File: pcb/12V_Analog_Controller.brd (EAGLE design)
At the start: 50 x 36 mm, 32 parts, among them J1 POWER, Q1 AO3400, Q2 AO3400, U1 ESP32-PICO-MINI-02, X1 PROG, X2 L1, X3 L2, X5 BOOT, X6 RESET

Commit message: Add second PTC footprint
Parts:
- added F3, F4: JK-SMD300L-24, M2M-Fuse:JK-SMD300
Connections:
- net N$5: now also F3.B
- net N$6: now also F4.B
- net VSW: now also F3.A, F4.A
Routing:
- net VSW: track 70.8 -> 79.6 mm
- net N$6: track 5.83 -> 12.8 mm
- net N$5: track 6.24 -> 13.2 mm
- net EN: track 27.3 -> 28.2 mm
- net L2: track 17.0 -> 17.9 mm
- net L1: track 17.5 -> 16.9 mm
- net VCC: track 35.3 -> 35.2 mm, vias 4 -> 3
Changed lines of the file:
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@@
 <drawing>
 <settings>
-<setting alwaysvectorfont="yes"/>
+<setting alwaysvectorfont="no"/>
 <setting verticaltext="up"/>
 </settings>
@@
 </element>
 <element name="X5" library="M2M-Connectors" package="1X02-2.54" value="BOOT" x="25.5" y="3.5" smashed="yes">
-<attribute name="NAME" x="24.23" y="5.0875" size="1.016" layer="25"/>
 <attribute name="NAME" x="24.611" y="2.865" size="1.27" layer="48"/>
 <attribute name="NAME" x="24.865" y="2.865" size="0.8128" layer="51"/>
+<attribute name="NAME" x="24.23" y="5.0875" size="1.016" layer="25"/>
 <attribute name="VALUE" x="24.23" y="0.96" size="1.016" layer="21"/>
 </element>
 <element name="X6" library="M2M-Connectors" package="1X02-2.54" value="RESET" x="19" y="3.5" smashed="yes">
-<attribute name="NAME" x="17.73" y="5.0875" size="1.016" layer="25"/>
 <attribute name="NAME" x="18.111" y="2.865" size="1.27" layer="48"/>
 <attribute name="NAME" x="18.865" y="2.365" size="0.8128" layer="51"/>
+<attribute name="NAME" x="17.73" y="5.0875" size="1.016" layer="25"/>
 <attribute name="VALUE" x="17.73" y="0.96" size="1.016" layer="21"/>
 </element>
@@
 <attribute name="NAME" x="34" y="7.8" size="1.016" layer="21"/>
 <attribute name="VALUE" x="34" y="4.2" size="1.016" layer="27"/>
+</element>
+<element name="F3" library="M2M-Fuse" package="JK-SMD300" value="JK-SMD300L-24" x="21" y="25" smashed="yes" rot="MR90">
+<attribute name="NAME" x="24.5" y="20" size="1.016" layer="26" rot="MR90"/>
+<attribute name="NAME" x="21" y="25" size="1.016" layer="48" rot="MR90" align="center"/>
+<attribute name="VALUE" x="16.5" y="20" size="1.016" layer="28" rot="MR90"/>
+</element>
+<element name="F4" library="M2M-Fuse" package="JK-SMD300" value="JK-SMD300L-24" x="21" y="11" smashed="yes" rot="MR90">
+<attribute name="NAME" x="24.5" y="6" size="1.016" layer="26" rot="MR90"/>
+<attribute name="NAME" x="21" y="11" size="1.016" layer="48" rot="MR90" align="center"/>
+<attribute name="VALUE" x="16.5" y="6" size="1.016" layer="28" rot="MR90"/>
 </element>
 </elements>
@@
 <vertex x="20.3" y="11.7"/>
 </polygon>
-<wire x1="22.5" y1="12.35" x2="22.5" y2="13.1298" width="0.254" layer="1"/>
-<via x="22.5" y="13.1298" extent="1-16" drill="0.35"/>
 <via x="27.5" y="11.5" extent="1-16" drill="0.35"/>
 <wire x1="27.5" y1="11.5" x2="27.15" y2="10.85" width="0.254" layer="1"/>
 <wire x1="27.15" y1="10.85" x2="26.5" y2="10.85" width="0.254" layer="1"/>
-<wire x1="22.5" y1="13.1298" x2="22.6298" y2="13" width="0.254" layer="16"/>
-<wire x1="26" y1="13" x2="27.5" y2="11.5" width="0.254" layer="16"/>
-<wire x1="26" y1="13" x2="22.6298" y2="13" width="0.254" layer="16"/>
 <wire x1="20.5" y1="12.35" x2="19.5" y2="11.35" width="0.254" layer="1"/>
 <wire x1="19.5" y1="7.85" x2="20" y2="7.35" width="0.254" layer="1"/>
@@
 <wire x1="28.1" y1="26.9" x2="25.75" y2="26.9" width="0.6096" layer="1"/>
 <wire x1="25.75" y1="26.9" x2="25.5" y2="26.65" width="0.6096" layer="1"/>
-<wire x1="20.5" y1="12.35" x2="20.5" y2="13" width="0.6096" layer="1"/>
-<via x="20.5" y="13" extent="1-16" drill="0.35"/>
-<wire x1="20.5" y1="23" x2="20.5" y2="13" width="0.6096" layer="16"/>
-<wire x1="20.5" y1="23" x2="24" y2="26.5" width="0.6096" layer="16"/>
 <via x="24" y="26.5" extent="1-16" drill="0.35"/>
 <wire x1="24" y1="26.5" x2="24.15" y2="26.65" width="0.6096" layer="1"/>
 <wire x1="24.15" y1="26.65" x2="25.5" y2="26.65" width="0.6096" layer="1"/>
+<wire x1="20.5" y1="12.35" x2="21.35" y2="12.35" width="0.6096" layer="1"/>
+<wire x1="21.35" y1="12.35" x2="21.5" y2="12.5" width="0.6096" layer="1"/>
+<via x="21.5" y="12.5" extent="1-16" drill="0.35"/>
+<wire x1="21.5" y1="12.5" x2="23.5" y2="12.5" width="0.6096" layer="16"/>
+<wire x1="23.5" y1="12.5" x2="23.75" y2="12.75" width="0.6096" layer="16"/>
+<wire x1="23.75" y1="12.75" x2="24.5" y2="13.5" width="0.6096" layer="16"/>
+<wire x1="24.5" y1="26" x2="24" y2="26.5" width="0.6096" layer="16"/>
+<wire x1="24.5" y1="13.5" x2="24.5" y2="26" width="0.6096" layer="16"/>
+<wire x1="27.5" y1="11.5" x2="26.25" y2="12.75" width="0.254" layer="16"/>
+<wire x1="26.25" y1="12.75" x2="23.75" y2="12.75" width="0.254" layer="16"/>
 </signal>
 <signal name="GND">
@@
 <via x="40" y="18.5" extent="1-16" drill="0.35"/>
 <via x="31" y="18.5" extent="1-16" drill="0.35"/>
-<via x="27.119" y="19.643" extent="1-16" drill="0.35"/>
+<via x="28.119" y="18.643" extent="1-16" drill="0.35"/>
 <via x="47.5" y="2.5" extent="1-16" drill="0.35"/>
 <via x="46" y="23" extent="1-16" drill="0.35"/>
@@
 <via x="10.5" y="27" extent="1-16" drill="0.35"/>
 <via x="32" y="16" extent="1-16" drill="0.35"/>
-<via x="23.5" y="8" extent="1-16" drill="0.35"/>
+<via x="25.5" y="8.5" extent="1-16" drill="0.35"/>
 <via x="29.5" y="7" extent="1-16" drill="0.35"/>
-<via x="18.5" y="8.5" extent="1-16" drill="0.35"/>
-<via x="18.5" y="22.5" extent="1-16" drill="0.35"/>
+<via x="18" y="9" extent="1-16" drill="0.35"/>
+<via x="19.5" y="24" extent="1-16" drill="0.35"/>
 <contactref element="C2" pad="2"/>
 <contactref element="U$3" pad="2"/>
@@
 <contactref element="R8" pad="1"/>
 <contactref element="C4" pad="2"/>
+<via x="19" y="12.5" extent="1-16" drill="0.35"/>
 </signal>
 <signal name="IO0">
@@
 <wire x1="19" y1="3.5" x2="20" y2="4.5" width="0.254" layer="1"/>
 <wire x1="20" y1="4.5" x2="20" y2="5.65" width="0.254" layer="1"/>
-<wire x1="26.5" y1="22" x2="26.5" y2="20" width="0.254" layer="1"/>
-<wire x1="25.5" y1="19" x2="24" y2="19" width="0.254" layer="1"/>
-<wire x1="24" y1="19" x2="17.5" y2="12.5" width="0.254" layer="1"/>
-<wire x1="17.5" y1="12.5" x2="17.497340625" y2="12.002659375" width="0.254" layer="1"/>
+<wire x1="26.5" y1="19.5" x2="26.5" y2="22" width="0.254" layer="1"/>
 <via x="17.497340625" y="12.002659375" extent="1-16" drill="0.35"/>
 <wire x1="17.497340625" y1="12.002659375" x2="17.497340625" y2="10.497340625" width="0.254" layer="16"/>
 <wire x1="17.497340625" y1="10.497340625" x2="17" y2="10" width="0.254" layer="16"/>
 <via x="17" y="10" extent="1-16" drill="0.35"/>
-<wire x1="26.5" y1="20" x2="25.5" y2="19" width="0.254" layer="1"/>
 <wire x1="19.35" y1="5.65" x2="20" y2="5.65" width="0.254" layer="1"/>
 <wire x1="17" y1="10" x2="17" y2="8" width="0.254" layer="1"/>
 <wire x1="17" y1="8" x2="19.35" y2="5.65" width="0.254" layer="1"/>
+<wire x1="17.497340625" y1="12.002659375" x2="17.497340625" y2="13.497340625" width="0.254" layer="1"/>
+<wire x1="25.8" y1="18.8" x2="26.5" y2="19.5" width="0.254" layer="1"/>
+<wire x1="17.497340625" y1="13.497340625" x2="22.8" y2="18.8" width="0.254" layer="1"/>
+<wire x1="22.8" y1="18.8" x2="25.8" y2="18.8" width="0.254" layer="1"/>
 </signal>
 <signal name="TXD0">
@@
 <wire x1="19" y1="27" x2="16.35" y2="27" width="0.254" layer="1"/>
 <contactref element="U1" pad="12"/>
-<wire x1="24" y1="22" x2="19" y2="27" width="0.254" layer="1"/>
+<wire x1="25.5" y1="20.5" x2="19" y2="27" width="0.254" layer="1"/>
 <wire x1="29.2" y1="19.6" x2="29.2" y2="20.2" width="0.254" layer="1"/>
 <wire x1="29.2" y1="20.2" x2="29.5" y2="20.5" width="0.254" layer="1"/>
 <via x="29.5" y="20.5" extent="1-16" drill="0.35"/>
-<wire x1="29.5" y1="20.5" x2="24.5" y2="20.5" width="0.254" layer="16"/>
-<via x="24.5" y="20.5" extent="1-16" drill="0.35"/>
-<wire x1="24.5" y1="20.5" x2="24" y2="21" width="0.254" layer="1"/>
-<wire x1="24" y1="21" x2="24" y2="22" width="0.254" layer="1"/>
+<wire x1="29.5" y1="20.5" x2="25.5" y2="20.5" width="0.254" layer="16"/>
+<via x="25.5" y="20.5" extent="1-16" drill="0.35"/>
 </signal>
 <signal name="L2">
@@
 <wire x1="30" y1="19.6" x2="30" y2="18.5" width="0.254" layer="1"/>
 <via x="30" y="18.5" extent="1-16" drill="0.35"/>
-<wire x1="30" y1="18.5" x2="22" y2="18.5" width="0.254" layer="16"/>
-<via x="22" y="18.5" extent="1-16" drill="0.35"/>
-<wire x1="16.5" y1="13" x2="16.35" y2="13" width="0.254" layer="1"/>
-<wire x1="22" y1="18.5" x2="16.5" y2="13" width="0.254" layer="1"/>
+<wire x1="30" y1="18.5" x2="29" y2="19.5" width="0.254" layer="16"/>
+<wire x1="29" y1="19.5" x2="25.5" y2="19.5" width="0.254" layer="16"/>
+<via x="25.5" y="19.5" extent="1-16" drill="0.35"/>
+<wire x1="16.35" y1="13" x2="22.85" y2="19.5" width="0.254" layer="1"/>
+<wire x1="22.85" y1="19.5" x2="25.5" y2="19.5" width="0.254" layer="1"/>
 </signal>
 <signal name="NC">
@@
 <wire x1="14" y1="28.7" x2="9.8" y2="24.5" width="1.5" layer="16"/>
 <wire x1="9.8" y1="24.5" x2="9.5" y2="24.5" width="1.5" layer="16"/>
+<contactref element="F3" pad="B"/>
+<wire x1="14" y1="28.7" x2="21" y2="28.7" width="1.016" layer="16"/>
 </signal>
 <signal name="N$6">
@@
 <wire x1="14" y1="14.7" x2="10.8" y2="11.5" width="1.5" layer="16"/>
 <wire x1="10.8" y1="11.5" x2="9.5" y2="11.5" width="1.5" layer="16"/>
+<contactref element="F4" pad="B"/>
+<wire x1="14" y1="14.7" x2="21" y2="14.7" width="1.016" layer="16"/>
 </signal>
 <signal name="N$7">
@@
 <contactref element="F2" pad="A"/>
 <wire x1="15.8" y1="5.5" x2="14" y2="7.3" width="1.5" layer="16"/>
-<wire x1="36.04" y1="5.5" x2="32" y2="5.5" width="1.5" layer="16"/>
-<wire x1="32" y1="5.5" x2="15.8" y2="5.5" width="1.5" layer="16"/>
+<wire x1="36.04" y1="5.5" x2="21" y2="5.5" width="1.5" layer="16"/>
+<wire x1="21" y1="5.5" x2="15.8" y2="5.5" width="1.5" layer="16"/>
 <wire x1="4.5" y1="17" x2="1.5" y2="14" width="1.5" layer="16"/>
 <wire x1="1.5" y1="14" x2="1.5" y2="7.5" width="1.5" layer="16"/>
@@
 <wire x1="37.525" y1="7.025" x2="40.5" y2="10" width="0.6096" layer="1"/>
 <wire x1="9.7" y1="17" x2="14" y2="21.3" width="1.5" layer="16"/>
+<contactref element="F3" pad="A"/>
+<contactref element="F4" pad="A"/>
+<wire x1="14" y1="21.3" x2="21" y2="21.3" width="1.016" layer="16"/>
+<wire x1="21" y1="7.3" x2="21" y2="5.5" width="0.6096" layer="16"/>
 </signal>
 </signals>

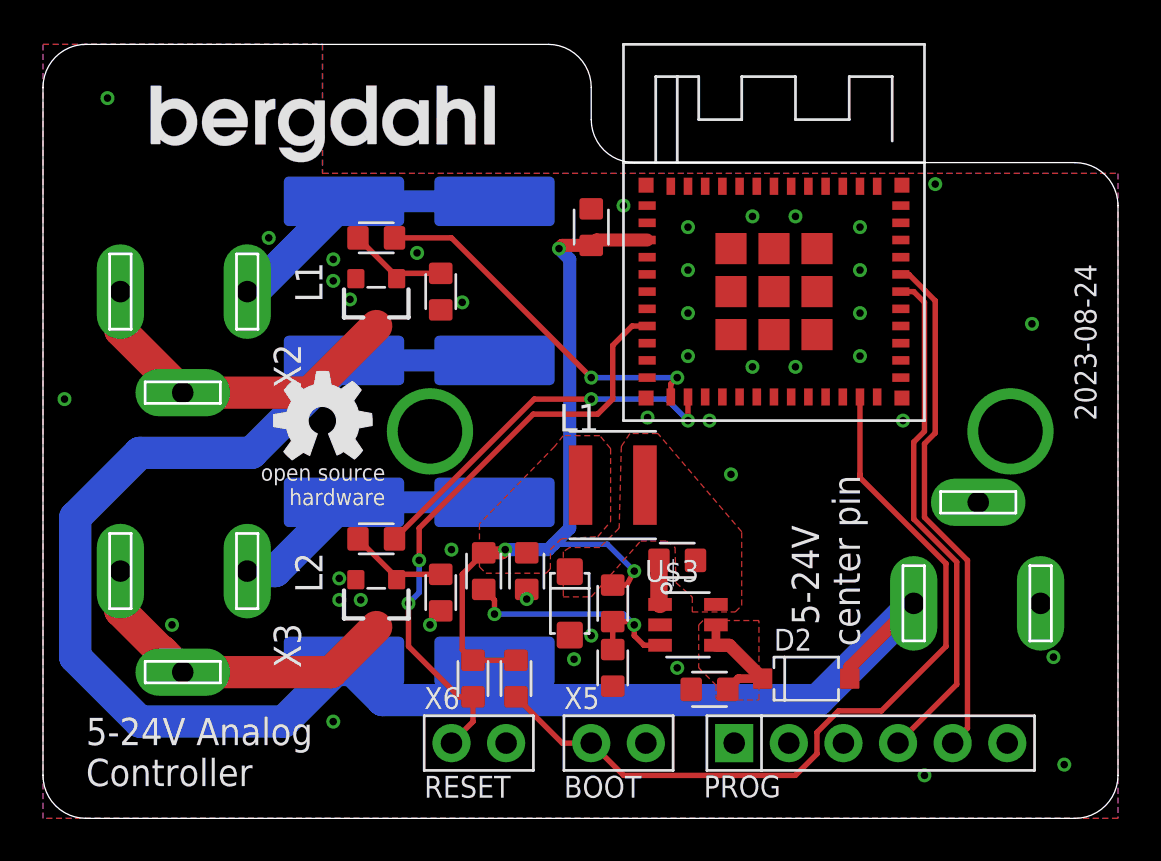
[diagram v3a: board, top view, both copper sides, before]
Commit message: Increase current capablity
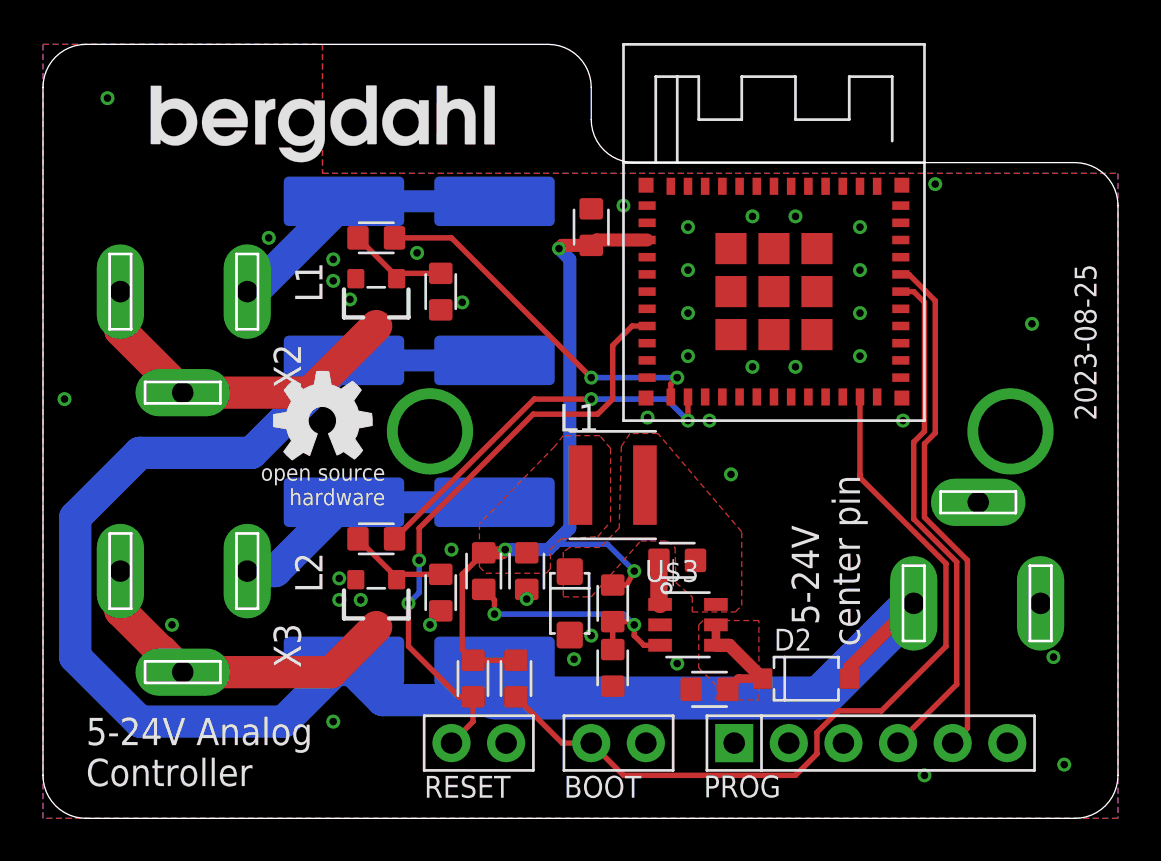
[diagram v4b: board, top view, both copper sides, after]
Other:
- board text added: "2023-08-25"
- board text removed: "2023-08-24"
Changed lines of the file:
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@@
 <drawing>
 <settings>
-<setting alwaysvectorfont="no"/>
+<setting alwaysvectorfont="yes"/>
 <setting verticaltext="up"/>
 </settings>
@@
 <text x="2" y="1.5" size="1.27" layer="21">5-24V Analog
 Controller </text>
-<text x="49" y="18.5" size="1.016" layer="21" rot="R90">2023-08-24</text>
+<text x="49" y="18.5" size="1.016" layer="21" rot="R90">2023-08-25</text>
 <text x="38" y="8" size="1.27" layer="21" rot="R90">  5-24V
 center pin</text>
@@
 </element>
 <element name="X5" library="M2M-Connectors" package="1X02-2.54" value="BOOT" x="25.5" y="3.5" smashed="yes">
+<attribute name="NAME" x="24.23" y="5.0875" size="1.016" layer="25"/>
 <attribute name="NAME" x="24.611" y="2.865" size="1.27" layer="48"/>
 <attribute name="NAME" x="24.865" y="2.865" size="0.8128" layer="51"/>
-<attribute name="NAME" x="24.23" y="5.0875" size="1.016" layer="25"/>
 <attribute name="VALUE" x="24.23" y="0.96" size="1.016" layer="21"/>
 </element>
 <element name="X6" library="M2M-Connectors" package="1X02-2.54" value="RESET" x="19" y="3.5" smashed="yes">
+<attribute name="NAME" x="17.73" y="5.0875" size="1.016" layer="25"/>
 <attribute name="NAME" x="18.111" y="2.865" size="1.27" layer="48"/>
 <attribute name="NAME" x="18.865" y="2.365" size="0.8128" layer="51"/>
-<attribute name="NAME" x="17.73" y="5.0875" size="1.016" layer="25"/>
 <attribute name="VALUE" x="17.73" y="0.96" size="1.016" layer="21"/>
 </element>
@@
 <via x="32" y="16" extent="1-16" drill="0.35"/>
 <via x="25.5" y="8.5" extent="1-16" drill="0.35"/>
-<via x="29.5" y="7" extent="1-16" drill="0.35"/>
+<via x="29.5" y="7.2" extent="1-16" drill="0.35"/>
 <via x="18" y="9" extent="1-16" drill="0.35"/>
 <via x="19.5" y="24" extent="1-16" drill="0.35"/>
@@
 <contactref element="F2" pad="A"/>
 <wire x1="15.8" y1="5.5" x2="14" y2="7.3" width="1.5" layer="16"/>
-<wire x1="36.04" y1="5.5" x2="21" y2="5.5" width="1.5" layer="16"/>
+<wire x1="36.14" y1="5.6" x2="21" y2="5.6" width="2" layer="16"/>
 <wire x1="21" y1="5.5" x2="15.8" y2="5.5" width="1.5" layer="16"/>
 <wire x1="4.5" y1="17" x2="1.5" y2="14" width="1.5" layer="16"/>
@@
 <wire x1="4.5" y1="4.5" x2="11.2" y2="4.5" width="1.5" layer="16"/>
 <wire x1="40.5" y1="10" x2="40.5" y2="9.96" width="1.5" layer="16"/>
-<wire x1="40.5" y1="9.96" x2="36.04" y2="5.5" width="1.5" layer="16"/>
+<wire x1="40.5" y1="9.96" x2="36.14" y2="5.6" width="2" layer="16"/>
 <wire x1="37.525" y1="6.5" x2="37.525" y2="7.025" width="0.6096" layer="1"/>
 <wire x1="37.525" y1="7.025" x2="40.5" y2="10" width="0.6096" layer="1"/>
@@
 <contactref element="F4" pad="A"/>
 <wire x1="14" y1="21.3" x2="21" y2="21.3" width="1.016" layer="16"/>
-<wire x1="21" y1="7.3" x2="21" y2="5.5" width="0.6096" layer="16"/>
+<wire x1="21" y1="7.3" x2="21" y2="5.6" width="0.6096" layer="16"/>
+<wire x1="21" y1="5.6" x2="21" y2="5.5" width="0.6096" layer="16"/>
 </signal>
 </signals>
